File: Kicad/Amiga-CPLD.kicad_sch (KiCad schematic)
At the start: 21 parts, among them CN1 CDTV-DIAG, J1 JTAG, J2 LED, SW1 SW_DIP_x04, U1 AZ1117-3.3, U2 XC95144XL-TQ100, X1 50MHz

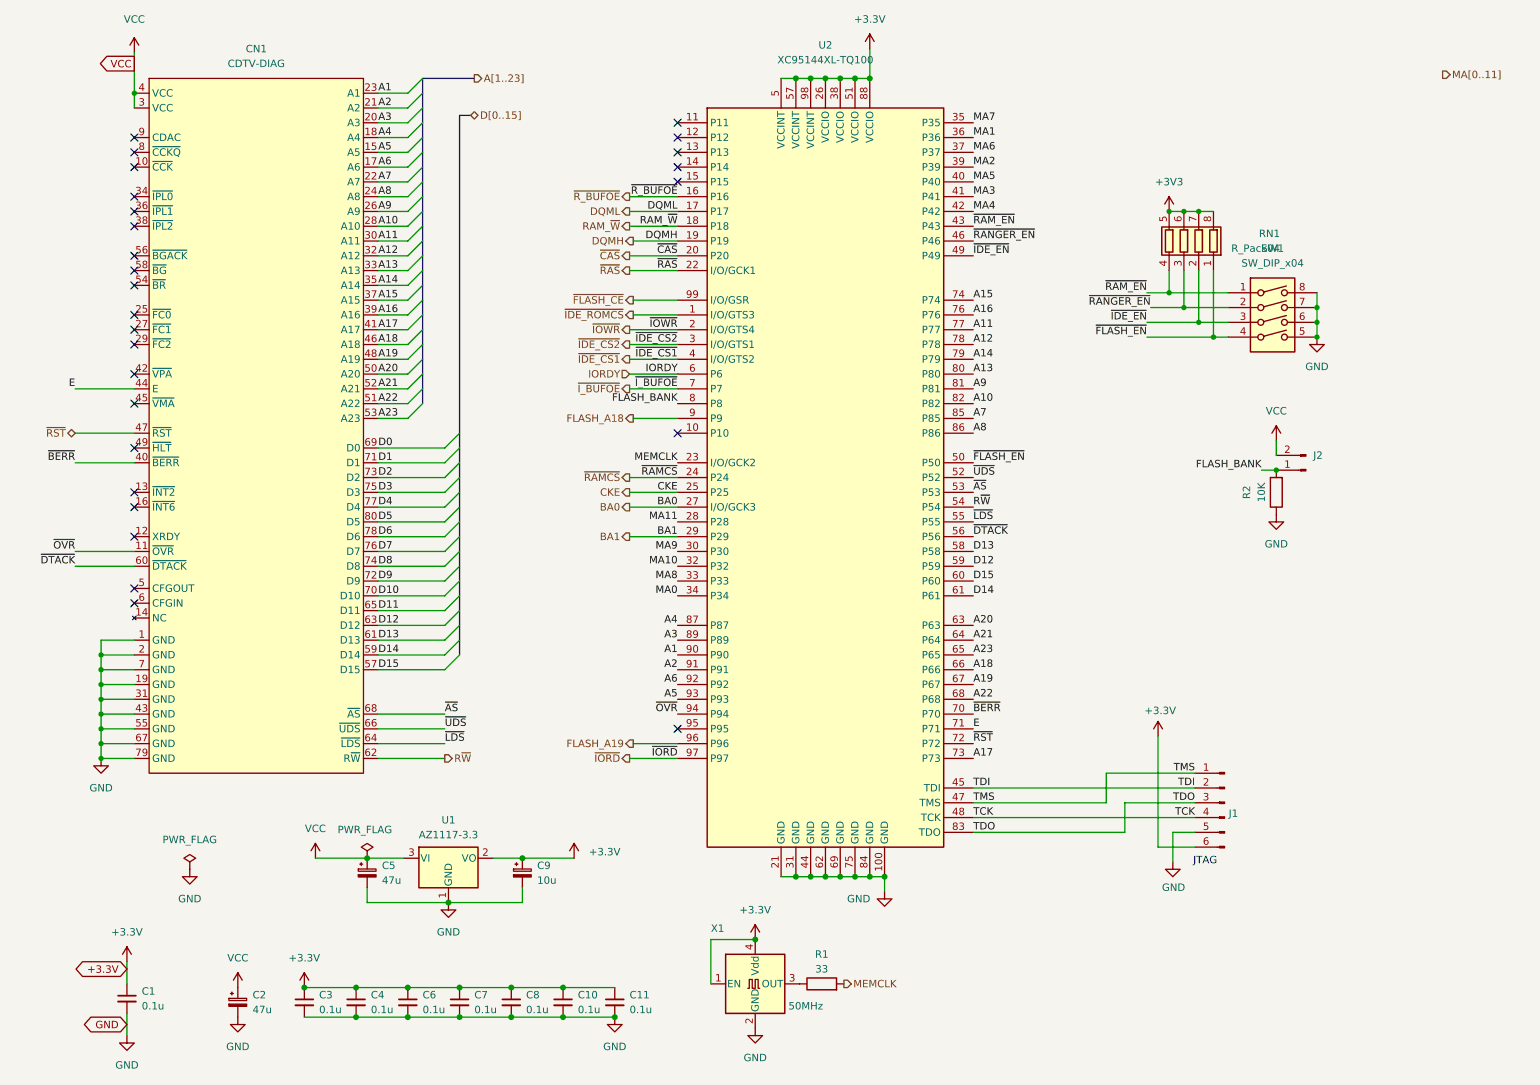
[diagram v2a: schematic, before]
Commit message: PCB: Fixups
* Tweak KEL connector hole sizes
* Fixup MT48LC8M16A2P - Had copied this from the 16M16 part and forgot to make A12 an NC
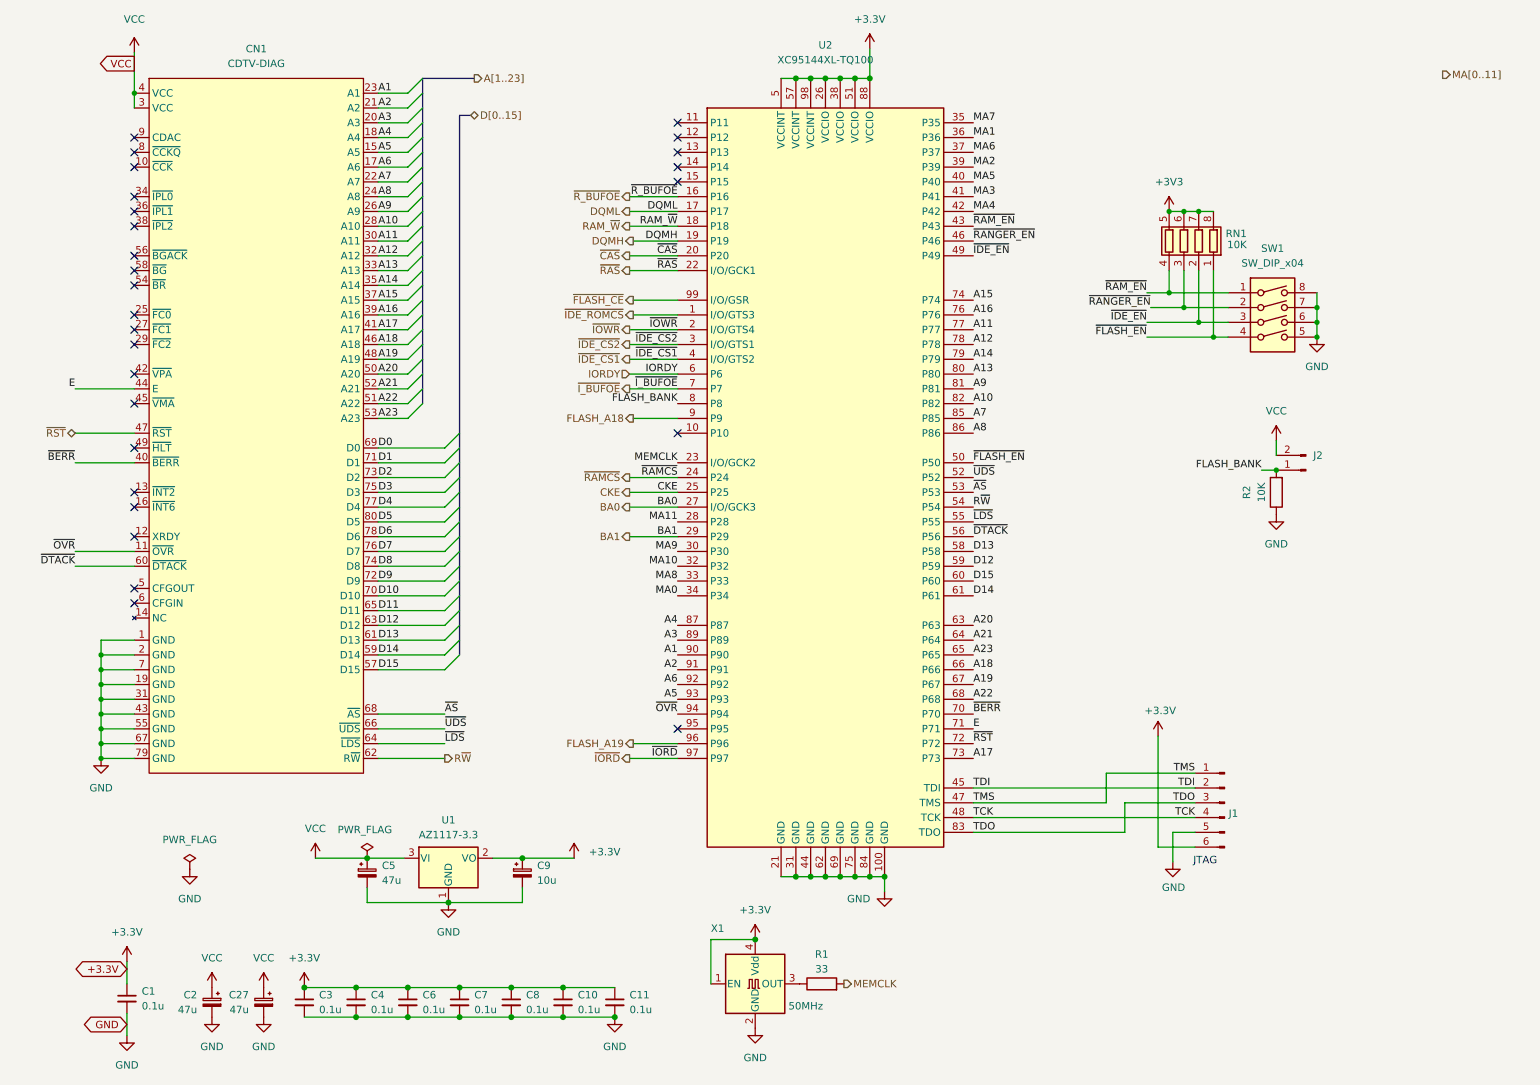
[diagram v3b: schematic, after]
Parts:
- added C27: 47u, Capacitor_Tantalum_SMD:CP_EIA-3216-18_Kemet-A, symbol Device:C_Polarized_Small
- RN1: value R_Pack04 -> 10K
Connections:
- net GND: now also C27.2
- net VCC: now also C27.1
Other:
- company: (none) -> Matt Harlum
- title: (none) -> CIDER
- moved on the sheet: C2
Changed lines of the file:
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@@
 (kicad_sch (version 20211123) (generator eeschema)
   (paper "A4")
+  (title_block
+    (title "CIDER")
+    (company "Matt Harlum")
+  )
   (junction (at 34.29 123.19) (diameter 0) (color 0 0 0 0)
   )
@@
     (pin "1")
   )
-  (symbol (lib_id "Device:C_Polarized_Small") (at 57.785 182.88 0) (unit 1)
-    (in_bom yes) (on_board yes) (fields_autoplaced)
-    (property "Reference" "C2" (id 0) (at 60.325 181.6099 0)
-      (effects (font (size 1.27 1.27)) (justify left))
-    )
-    (property "Value" "47u" (id 1) (at 60.325 184.1499 0)
-      (effects (font (size 1.27 1.27)) (justify left))
-    )
-    (property "Footprint" "Capacitor_Tantalum_SMD:CP_EIA-3216-18_Kemet-A" (id 2) (at 57.785 182.88 0)
-      (effects (font (size 1.27 1.27)) hide)
-    )
-    (property "Datasheet" "~" (id 3) (at 57.785 182.88 0)
-      (effects (font (size 1.27 1.27)) hide)
-    )
-    (property "LCSC #" "C193224" (id 4) (at 57.785 182.88 0)
+  (symbol (lib_id "Device:C_Polarized_Small") (at 53.34 182.88 0) (mirror y) (unit 1)
+    (in_bom yes) (on_board yes) (fields_autoplaced)
+    (property "Reference" "C2" (id 0) (at 50.8 181.6099 0)
+      (effects (font (size 1.27 1.27)) (justify left))
+    )
+    (property "Value" "47u" (id 1) (at 50.8 184.1499 0)
+      (effects (font (size 1.27 1.27)) (justify left))
+    )
+    (property "Footprint" "Capacitor_Tantalum_SMD:CP_EIA-3216-18_Kemet-A" (id 2) (at 53.34 182.88 0)
+      (effects (font (size 1.27 1.27)) hide)
+    )
+    (property "Datasheet" "~" (id 3) (at 53.34 182.88 0)
+      (effects (font (size 1.27 1.27)) hide)
+    )
+    (property "LCSC #" "C193224" (id 4) (at 53.34 182.88 0)
       (effects (font (size 1.27 1.27)) hide)
     )
@@
   (symbol (lib_id "Device:R_Pack04") (at 220.345 52.07 0) (mirror y) (unit 1)
     (in_bom yes) (on_board yes)
-    (property "Reference" "RN1" (id 0) (at 236.855 50.8 0)
-      (effects (font (size 1.27 1.27)) (justify left))
-    )
-    (property "Value" "R_Pack04" (id 1) (at 236.855 53.34 0)
+    (property "Reference" "RN1" (id 0) (at 231.14 50.8 0)
+      (effects (font (size 1.27 1.27)) (justify left))
+    )
+    (property "Value" "10K" (id 1) (at 231.14 52.705 0)
       (effects (font (size 1.27 1.27)) (justify left))
     )
@@
     (pin "1")
   )
-  (symbol (lib_id "power:GND") (at 57.785 185.42 0) (unit 1)
-    (in_bom yes) (on_board yes) (fields_autoplaced)
-    (property "Reference" "#PWR07" (id 0) (at 57.785 191.77 0)
-      (effects (font (size 1.27 1.27)) hide)
-    )
-    (property "Value" "GND" (id 1) (at 57.785 190.5 0))
-    (property "Footprint" "" (id 2) (at 57.785 185.42 0)
-      (effects (font (size 1.27 1.27)) hide)
-    )
-    (property "Datasheet" "" (id 3) (at 57.785 185.42 0)
+  (symbol (lib_id "power:GND") (at 53.34 185.42 0) (mirror y) (unit 1)
+    (in_bom yes) (on_board yes) (fields_autoplaced)
+    (property "Reference" "#PWR07" (id 0) (at 53.34 191.77 0)
+      (effects (font (size 1.27 1.27)) hide)
+    )
+    (property "Value" "GND" (id 1) (at 53.34 190.5 0))
+    (property "Footprint" "" (id 2) (at 53.34 185.42 0)
+      (effects (font (size 1.27 1.27)) hide)
+    )
+    (property "Datasheet" "" (id 3) (at 53.34 185.42 0)
       (effects (font (size 1.27 1.27)) hide)
     )
@@
     (pin "1")
   )
-  (symbol (lib_id "power:VCC") (at 57.785 180.34 0) (unit 1)
-    (in_bom yes) (on_board yes) (fields_autoplaced)
-    (property "Reference" "#PWR06" (id 0) (at 57.785 184.15 0)
-      (effects (font (size 1.27 1.27)) hide)
-    )
-    (property "Value" "VCC" (id 1) (at 57.785 175.26 0))
-    (property "Footprint" "" (id 2) (at 57.785 180.34 0)
-      (effects (font (size 1.27 1.27)) hide)
-    )
-    (property "Datasheet" "" (id 3) (at 57.785 180.34 0)
+  (symbol (lib_id "power:VCC") (at 53.34 180.34 0) (mirror y) (unit 1)
+    (in_bom yes) (on_board yes) (fields_autoplaced)
+    (property "Reference" "#PWR06" (id 0) (at 53.34 184.15 0)
+      (effects (font (size 1.27 1.27)) hide)
+    )
+    (property "Value" "VCC" (id 1) (at 53.34 175.26 0))
+    (property "Footprint" "" (id 2) (at 53.34 180.34 0)
+      (effects (font (size 1.27 1.27)) hide)
+    )
+    (property "Datasheet" "" (id 3) (at 53.34 180.34 0)
       (effects (font (size 1.27 1.27)) hide)
     )
@@
     (pin "1")
     (pin "2")
+  )
+  (symbol (lib_id "Device:C_Polarized_Small") (at 62.23 182.88 0) (mirror y) (unit 1)
+    (in_bom yes) (on_board yes) (fields_autoplaced)
+    (property "Reference" "C27" (id 0) (at 59.69 181.6099 0)
+      (effects (font (size 1.27 1.27)) (justify left))
+    )
+    (property "Value" "47u" (id 1) (at 59.69 184.1499 0)
+      (effects (font (size 1.27 1.27)) (justify left))
+    )
+    (property "Footprint" "Capacitor_Tantalum_SMD:CP_EIA-3216-18_Kemet-A" (id 2) (at 62.23 182.88 0)
+      (effects (font (size 1.27 1.27)) hide)
+    )
+    (property "Datasheet" "~" (id 3) (at 62.23 182.88 0)
+      (effects (font (size 1.27 1.27)) hide)
+    )
+    (property "LCSC #" "C193224" (id 4) (at 62.23 182.88 0)
+      (effects (font (size 1.27 1.27)) hide)
+    )
+    (pin "1")
+    (pin "2")
+  )
+  (symbol (lib_id "power:GND") (at 62.23 185.42 0) (mirror y) (unit 1)
+    (in_bom yes) (on_board yes) (fields_autoplaced)
+    (property "Reference" "#PWR061" (id 0) (at 62.23 191.77 0)
+      (effects (font (size 1.27 1.27)) hide)
+    )
+    (property "Value" "GND" (id 1) (at 62.23 190.5 0))
+    (property "Footprint" "" (id 2) (at 62.23 185.42 0)
+      (effects (font (size 1.27 1.27)) hide)
+    )
+    (property "Datasheet" "" (id 3) (at 62.23 185.42 0)
+      (effects (font (size 1.27 1.27)) hide)
+    )
+    (pin "1")
   )
   (symbol (lib_id "power:GND") (at 146.685 187.325 0) (unit 1)
@@
     (pin "2")
   )
+  (symbol (lib_id "power:VCC") (at 62.23 180.34 0) (mirror y) (unit 1)
+    (in_bom yes) (on_board yes) (fields_autoplaced)
+    (property "Reference" "#PWR060" (id 0) (at 62.23 184.15 0)
+      (effects (font (size 1.27 1.27)) hide)
+    )
+    (property "Value" "VCC" (id 1) (at 62.23 175.26 0))
+    (property "Footprint" "" (id 2) (at 62.23 180.34 0)
+      (effects (font (size 1.27 1.27)) hide)
+    )
+    (property "Datasheet" "" (id 3) (at 62.23 180.34 0)
+      (effects (font (size 1.27 1.27)) hide)
+    )
+    (pin "1")
+  )
   (symbol (lib_id "power:GND") (at 49.53 160.02 0) (unit 1)

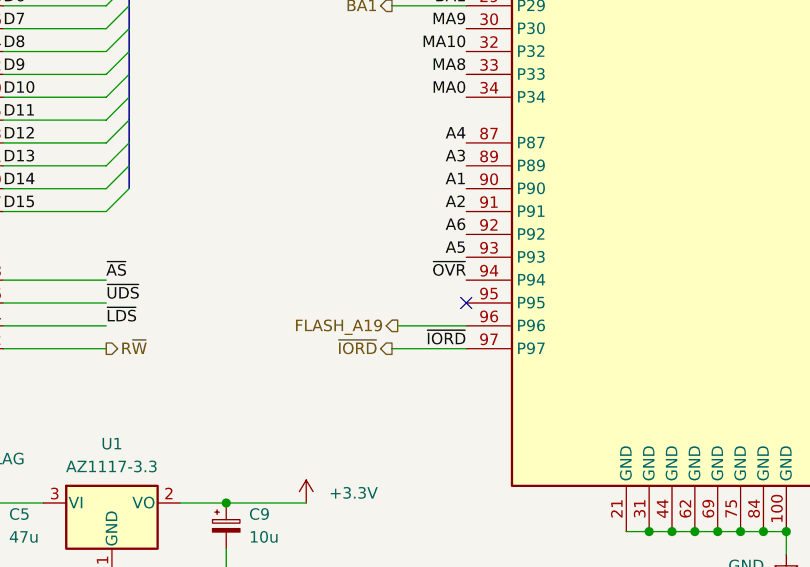
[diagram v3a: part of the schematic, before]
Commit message: PCB: Connect another CPLD pin to OVR_n
This should give more drive strength to make sure we can drive it low nice and fast
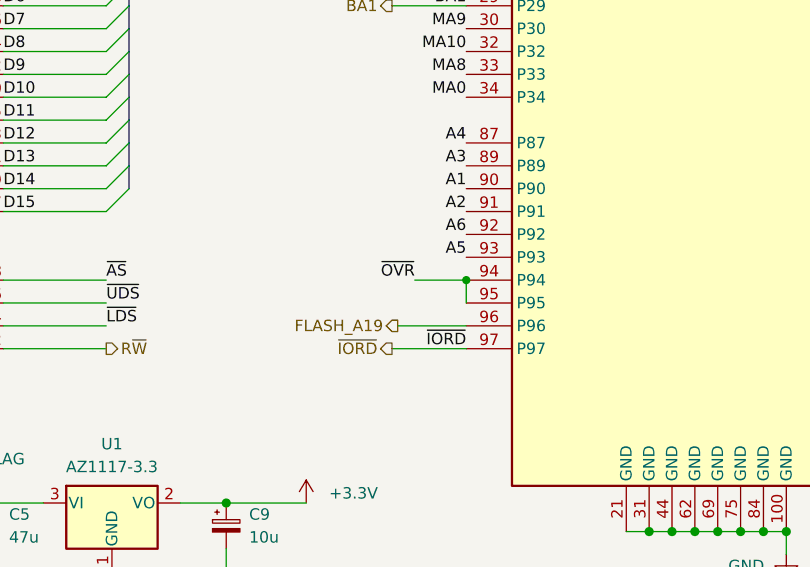
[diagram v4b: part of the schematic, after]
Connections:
- net ~{OVR}: now also U2.95 (P95)
- no-connect marks 27 -> 26
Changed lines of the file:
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@@
   (junction (at 166.37 161.29) (diameter 1.016) (color 0 0 0 0)
+  )
+  (junction (at 133.35 133.35) (diameter 0) (color 0 0 0 0)
   )
   (junction (at 217.805 60.96) (diameter 0) (color 0 0 0 0)
@@
   (no_connect (at 40.005 69.85))
   (no_connect (at 40.005 114.3))
-  (no_connect (at 133.35 135.89))
   (no_connect (at 40.005 95.25))
   (bus_entry (at 86.995 72.39) (size 2.54 -2.54)
@@
     (stroke (width 0) (type default) (color 0 0 0 0))
   )
+  (wire (pts (xy 127.635 133.35) (xy 133.35 133.35))
+    (stroke (width 0) (type default) (color 0 0 0 0))
+  )
   (wire (pts (xy 69.215 185.42) (xy 78.105 185.42))
     (stroke (width 0) (type solid) (color 0 0 0 0))
@@
     (stroke (width 0) (type solid) (color 0 0 0 0))
   )
+  (wire (pts (xy 133.35 133.35) (xy 133.35 135.89))
+    (stroke (width 0) (type default) (color 0 0 0 0))
+  )
   (wire (pts (xy 81.915 118.11) (xy 93.345 118.11))
     (stroke (width 0) (type default) (color 0 0 0 0))
@@
     (effects (font (size 1.27 1.27)) (justify left bottom))
   )
-  (label "~{OVR}" (at 133.35 133.35 180)
-    (effects (font (size 1.27 1.27)) (justify right bottom))
-  )
+  (label "~{OVR}" (at 127.635 133.35 180)
+    (effects (font (size 1.27 1.27)) (justify right bottom))
+  )
